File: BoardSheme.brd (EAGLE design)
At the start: 100 x 60 mm, 31 parts, among them IC1 7805DT, Q1 IRF540, Q2 IRF540, Q3 IRF540, Q4 IRF540, Q5 IRF540, Q6 IRF540

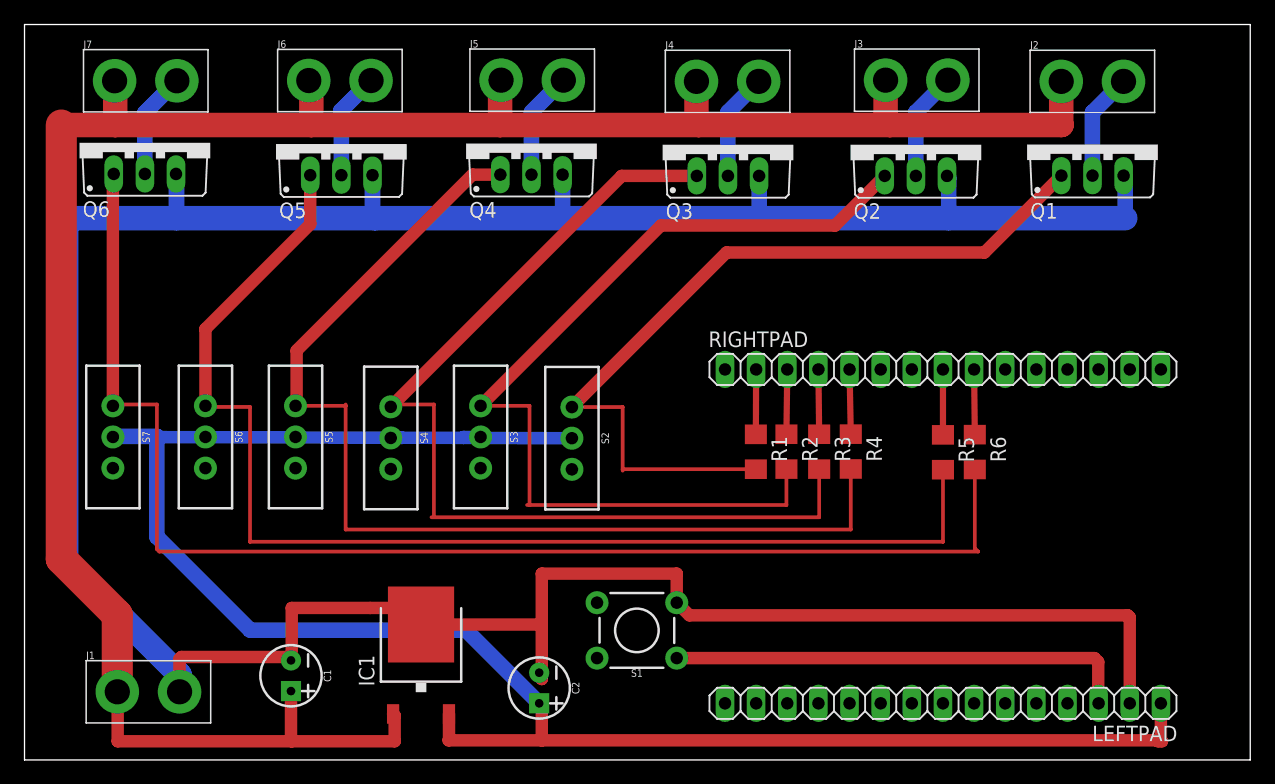
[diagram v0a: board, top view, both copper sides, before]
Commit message: small update to pcb
Made connections with power lines stronger
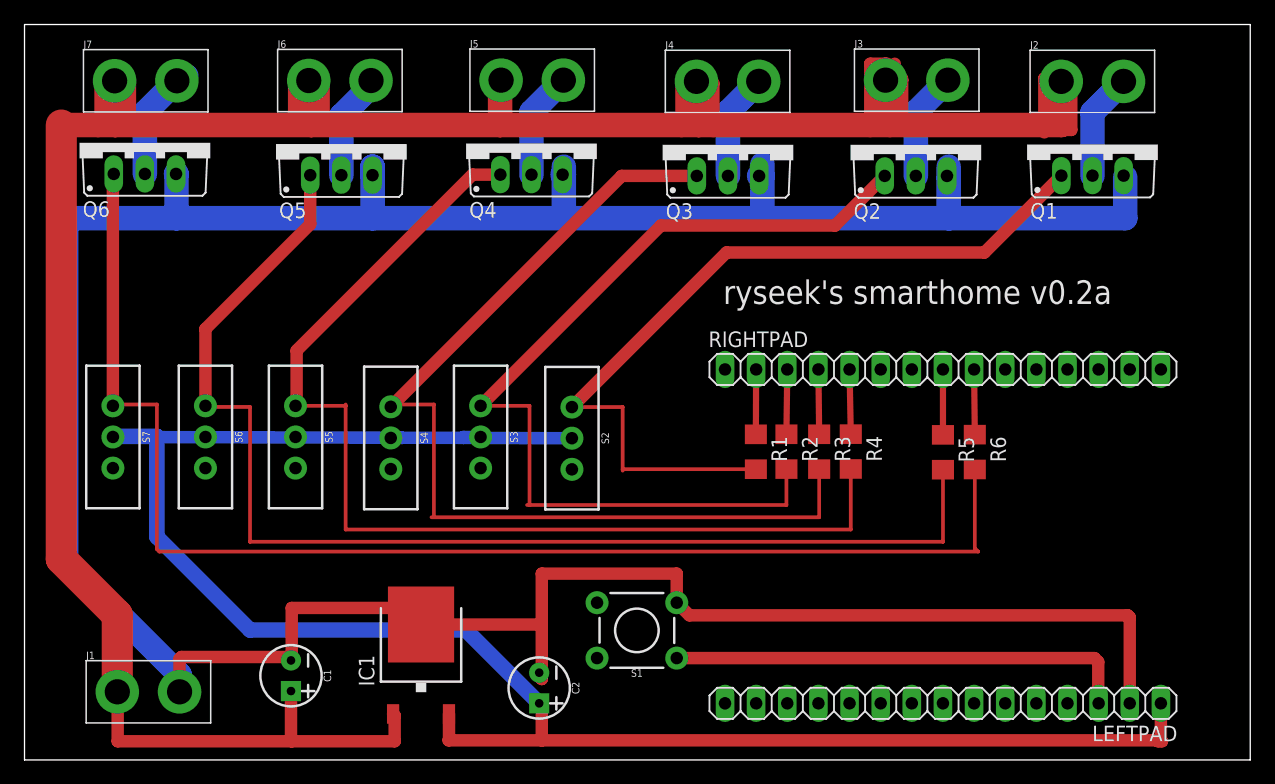
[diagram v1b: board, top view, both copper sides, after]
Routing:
- net +12V: track 184.8 -> 256.0 mm
- net GND: track 255.6 -> 259.9 mm
- net N$8: track 8.68 -> 10.4 mm
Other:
- board text added: "ryseek's smarthome v0.2a"
